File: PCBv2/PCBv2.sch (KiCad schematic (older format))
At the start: 76 parts, among them IC1 MAX743CWE+, J1 Arduino_Mega_Header, J10 Screw_Terminal_01x03, J11 Screw_Terminal_01x03, J12 Screw_Terminal_01x03, J13 Screw_Terminal_01x03, J2 Conn_01x10, J3 Conn_01x08, J4 Conn_01x08, J5 Conn_02x18_Odd_Even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

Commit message: Added photos of the prototype and changed the PCB
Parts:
- removed C20: 100nF, Cap:Cap, symbol C
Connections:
- net +15V: no longer U10.8 (V+)
- net -15V: no longer C19.2, U10.4 (V-)
- net 5V: now also C19.2, D5.1 (K), R20.2, R21.2, U10.8 (V+)
- net GND: now also U10.4 (V-)
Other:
- moved on the sheet: C19
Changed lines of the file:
@@
 L C C19
 U 1 1 5B011864
-P 10050 4750
-F 0 "C19" H 10075 4850 50  0000 L CNN
-F 1 "100nF" V 9900 4750 50  0000 L CNN
-F 2 "Cap:Cap" H 10088 4600 50  0001 C CNN
-F 3 "" H 10050 4750 50  0001 C CNN
-	1    10050 4750
-	0    1    1    0
+P 10050 5550
+F 0 "C19" H 10075 5650 50  0000 L CNN
+F 1 "100nF" V 9900 5550 50  0000 L CNN
+F 2 "Cap:Cap" H 10088 5400 50  0001 C CNN
+F 3 "" H 10050 5550 50  0001 C CNN
+	1    10050 5550
+	0    1    -1   0
 $EndComp
 Wire Wire Line
-	9900 4700 9900 4850
-Connection ~ 9900 4750
-Text Label 9900 4700 2    39   ~ 0
--15V
-Text Label 10200 4750 0    39   ~ 0
+	9900 5600 9900 5450
+Connection ~ 9900 5550
+Text Label 10200 5550 0    39   ~ 0
 GND
-$Comp
-L C C20
-U 1 1 5B011F3F
-P 10050 5500
-F 0 "C20" H 10075 5600 50  0000 L CNN
-F 1 "100nF" V 10200 5450 50  0000 L CNN
-F 2 "Cap:Cap" H 10088 5350 50  0001 C CNN
-F 3 "" H 10050 5500 50  0001 C CNN
-	1    10050 5500
-	0    1    1    0
-$EndComp
 Wire Wire Line
-	9900 5450 9900 5550
-Connection ~ 9900 5500
-Text Label 9900 5550 2    39   ~ 0
-+15V
-Text Label 10200 5500 0    39   ~ 0
-GND
+	9900 4850 9900 4750
 $Comp
 L R R23
@@
 	1    0    0    -1
 $EndComp
+Text Label 9900 4750 0    39   ~ 0
+GND
+Text Label 9900 5600 2    39   ~ 0
+5V
+Text Label 9150 5500 0    39   ~ 0
+5V
 $EndSCHEMATC

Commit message: Changes on PCB and pins of LCD
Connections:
- net PIN3: now also U1.2 (CE); no longer U1.1 (RST)
- net PIN4: now also U1.3 (DC); no longer U1.2 (CE)
- net PIN5: now also U1.4 (DIN); no longer U1.3 (DC)
- net PIN6: now also U1.5 (CLK); no longer U1.4 (DIN)
- net PIN2: now reaches J1.71 (PWM2/2)
- net PIN2: now also J3.6 (Pin_6), U1.1 (RST)
- removed net PIN7: J1.76 (PWM7/7), J3.1 (Pin_1), U1.5 (CLK)
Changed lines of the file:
@@
 Text Label 2500 950  0    39   ~ 0
 SDA
-Text Label 2500 1450 0    39   ~ 0
-PIN7
 Text Label 2500 1500 0    39   ~ 0
 PIN6
@@
 NoConn ~ 2200 1800
 NoConn ~ 2250 1750
-NoConn ~ 2200 1700
 NoConn ~ 2200 1350
 NoConn ~ 2250 1300
@@
 NoConn ~ 3050 2350
 NoConn ~ 3050 2250
-NoConn ~ 3050 2150
 Text Label 3050 2050 2    39   ~ 0
 PIN3
@@
 Text Label 3050 1750 2    39   ~ 0
 PIN6
-Text Label 3050 1650 2    39   ~ 0
-PIN7
 Text Label 3450 600  2    39   ~ 0
 SCL
@@
 $EndComp
 Text Label 6250 1100 2    39   ~ 0
+PIN2
+Text Label 6250 1200 2    39   ~ 0
 PIN3
-Text Label 6250 1200 2    39   ~ 0
+Text Label 6250 1300 2    39   ~ 0
 PIN4
-Text Label 6250 1300 2    39   ~ 0
+Text Label 6250 1400 2    39   ~ 0
 PIN5
-Text Label 6250 1400 2    39   ~ 0
+Text Label 6250 1500 2    39   ~ 0
 PIN6
-Text Label 6250 1500 2    39   ~ 0
-PIN7
 Text Label 6250 1600 2    39   ~ 0
 3.3V
@@
 Wire Wire Line
 	2200 950  2500 950
-Wire Wire Line
-	2250 1450 2500 1450
 Wire Wire Line
 	2200 1500 2500 1500
@@
 Text Label 9150 5500 0    39   ~ 0
 5V
+Wire Wire Line
+	2200 1700 2500 1700
+Text Label 2500 1700 0    39   ~ 0
+PIN2
+NoConn ~ 2250 1450
+NoConn ~ 3050 1650
+Text Label 3050 2150 2    39   ~ 0
+PIN2
 $EndSCHEMATC

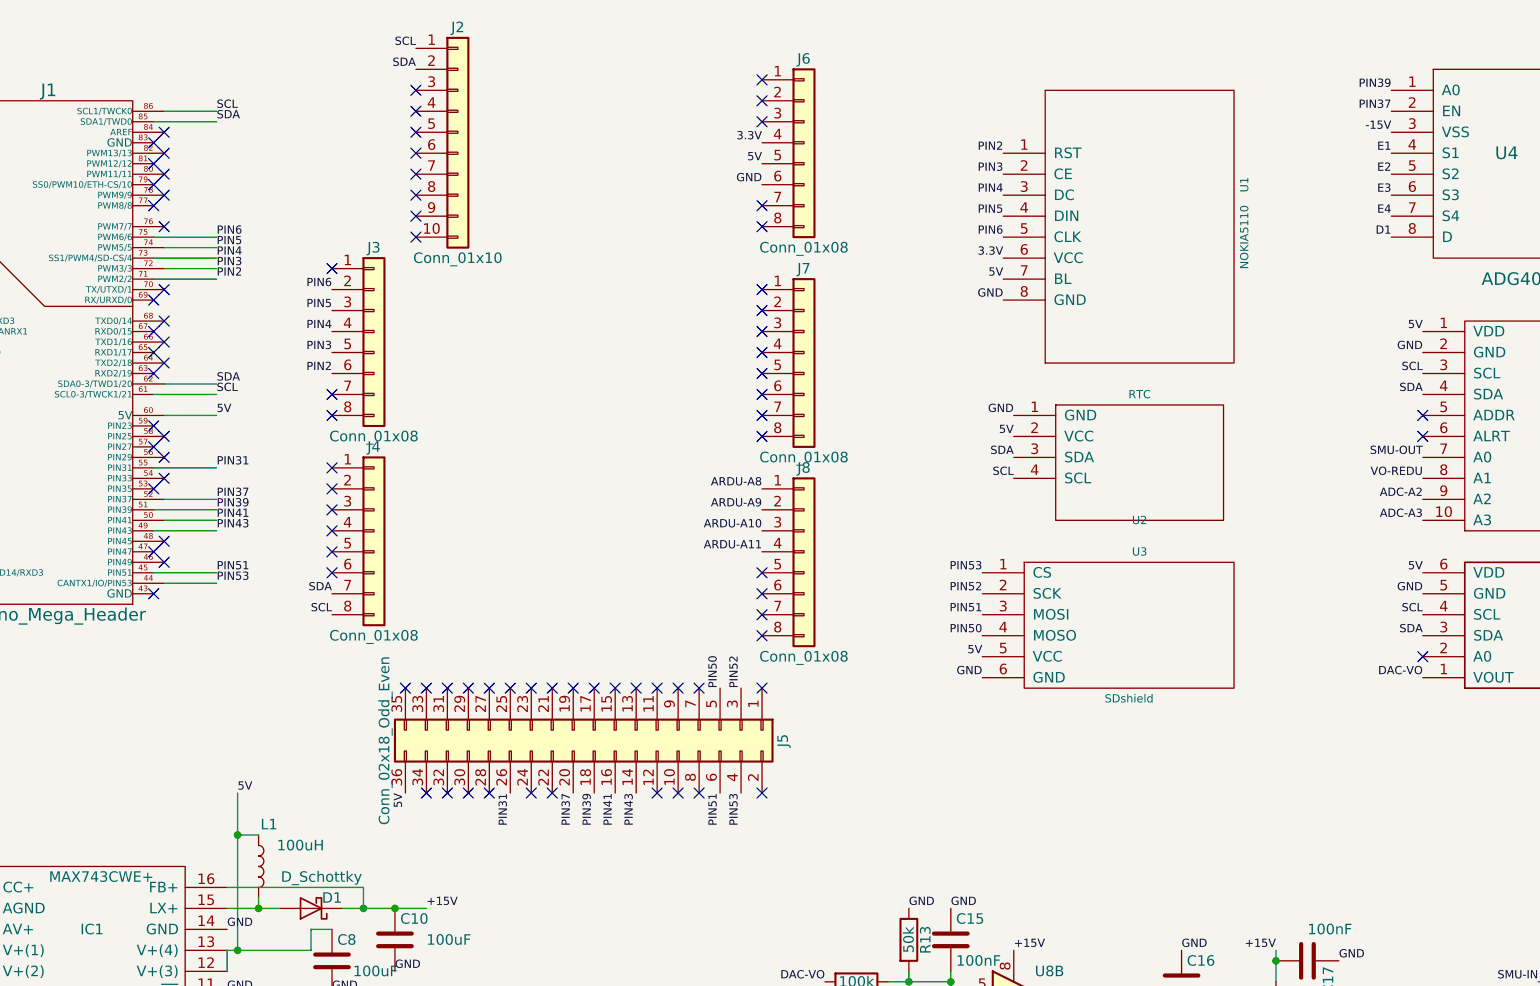
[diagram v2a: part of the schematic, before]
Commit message: Added GPRS communications and lots of changes on the main code!
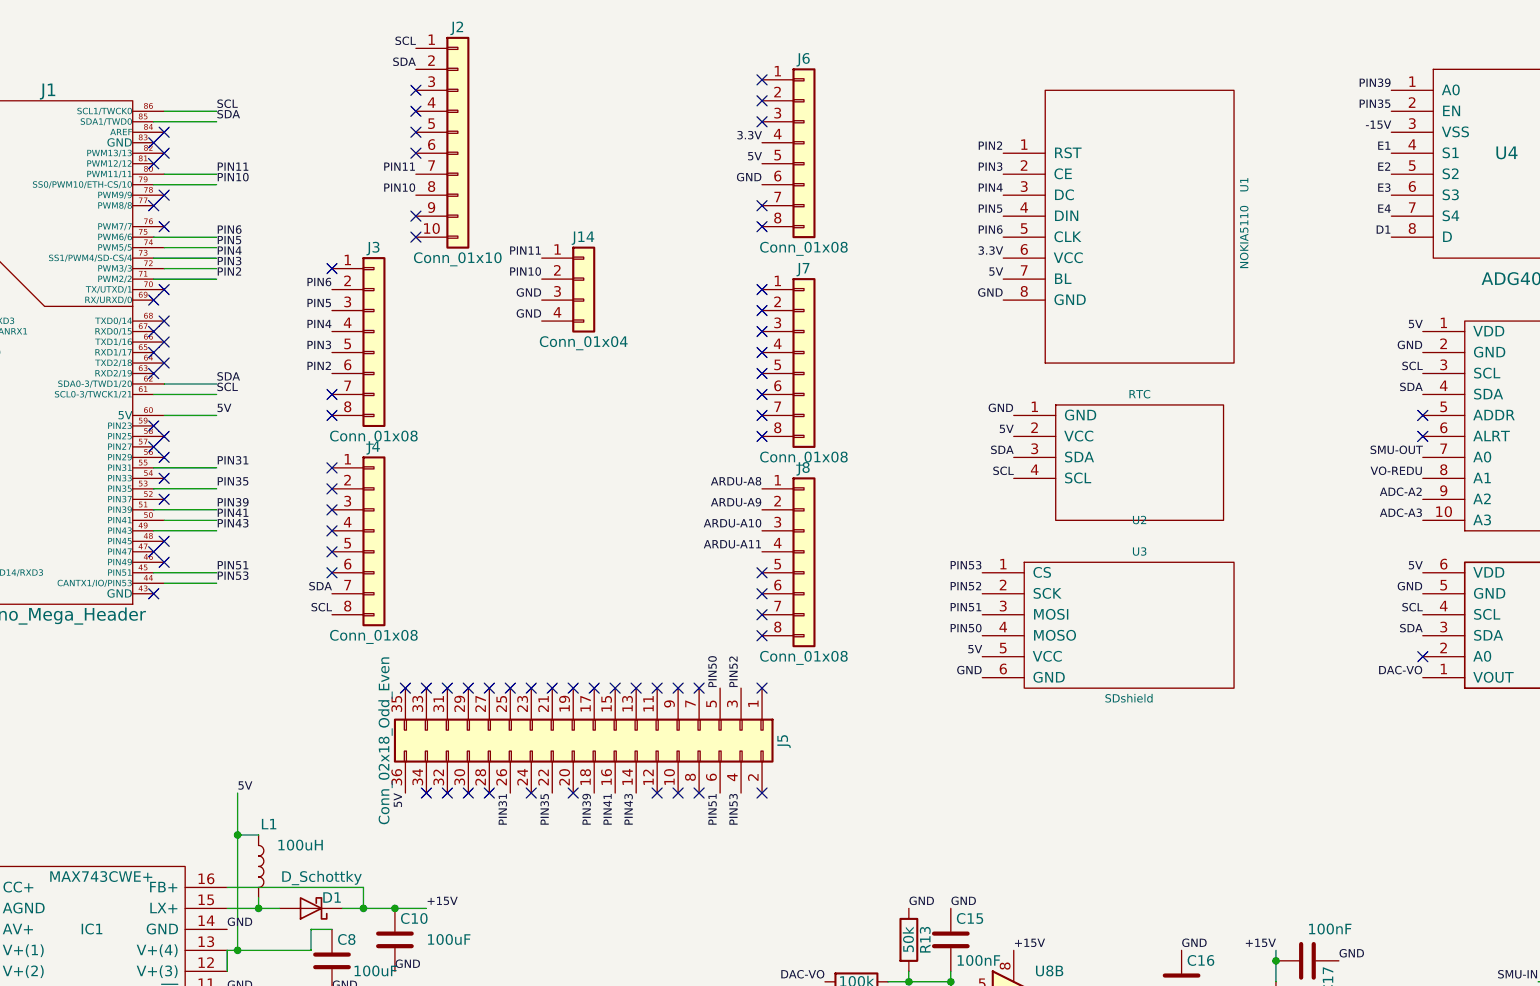
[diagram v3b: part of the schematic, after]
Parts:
- added J14: Conn_01x04, Pin_Headers:Pin_Header_Straight_1x04_Pitch2.54mm, symbol Conn_01x04
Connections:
- net GND: now also J14.3 (Pin_3), J14.4 (Pin_4)
- net PIN35: now reaches J1.53 (PIN35)
- net PIN35: now also J5.22 (Pin_22), U4.2 (EN)
- net PIN10: now reaches J1.79 (SS0/PWM10/ETH-CS/10)
- net PIN10: now also J2.8 (Pin_8), J14.2 (Pin_2)
- net PIN11: now reaches J1.80 (PWM11/11)
- net PIN11: now also J2.7 (Pin_7), J14.1 (Pin_1)
- removed net PIN37: J1.52 (PIN37), J5.20 (Pin_20), U4.2 (EN)
- no-connect marks 122 -> 118
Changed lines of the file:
@@
 Text Label 2500 2350 0    39   ~ 0
 5V
-Text Label 2500 2750 0    39   ~ 0
-PIN37
 Text Label 2500 2800 0    39   ~ 0
 PIN39
@@
 NoConn ~ 2200 3000
 NoConn ~ 2250 2950
-NoConn ~ 2200 2700
 NoConn ~ 2250 2650
 NoConn ~ 2250 2550
@@
 NoConn ~ 2200 1350
 NoConn ~ 2250 1300
-NoConn ~ 2200 1250
-NoConn ~ 2250 1200
 NoConn ~ 2200 1150
 NoConn ~ 2250 1100
@@
 Text Label 4400 4150 3    39   ~ 0
 PIN41
-Text Label 4200 4150 3    39   ~ 0
-PIN37
 Text Label 3900 4150 3    39   ~ 0
 PIN31
@@
 NoConn ~ 3800 4150
 NoConn ~ 4000 4150
-NoConn ~ 4100 4150
 $Comp
 L Conn_01x08 J4
@@
 NoConn ~ 3450 1000
 NoConn ~ 3450 1100
-NoConn ~ 3450 1200
-NoConn ~ 3450 1300
 $Comp
 L Conn_01x10 J2
@@
 Text Label 8100 800  2    39   ~ 0
 PIN39
-Text Label 8100 900  2    39   ~ 0
-PIN37
 Text Label 8100 1000 2    39   ~ 0
 -15V
@@
 Wire Wire Line
 	2200 2800 2500 2800
-Wire Wire Line
-	2250 2750 2500 2750
 Wire Wire Line
 	2250 2350 2500 2350
@@
 Text Label 3050 2150 2    39   ~ 0
 PIN2
+Wire Wire Line
+	2250 1200 2500 1200
+Wire Wire Line
+	2200 1250 2500 1250
+Text Label 2500 1200 0    39   ~ 0
+PIN11
+Text Label 2500 1250 0    39   ~ 0
+PIN10
+Text Label 4050 1600 2    39   ~ 0
+PIN11
+Text Label 4050 1700 2    39   ~ 0
+PIN10
+Text Label 4050 1800 2    39   ~ 0
+GND
+$Comp
+L Conn_01x04 J14
+U 1 1 5B0C0681
+P 4250 1700
+F 0 "J14" H 4250 1900 50  0000 C CNN
+F 1 "Conn_01x04" H 4250 1400 50  0000 C CNN
+F 2 "Pin_Headers:Pin_Header_Straight_1x04_Pitch2.54mm" H 4250 1700 50  0001 C CNN
+F 3 "" H 4250 1700 50  0001 C CNN
+	1    4250 1700
+	1    0    0    -1
+$EndComp
+Text Label 4050 1900 2    39   ~ 0
+GND
+Text Label 3450 1200 2    39   ~ 0
+PIN11
+Text Label 3450 1300 2    39   ~ 0
+PIN10
+NoConn ~ 2250 2750
+Wire Wire Line
+	2200 2700 2500 2700
+Text Label 2500 2700 0    39   ~ 0
+PIN35
+NoConn ~ 4200 4150
+Text Label 4100 4150 3    39   ~ 0
+PIN35
+Text Label 8100 900  2    39   ~ 0
+PIN35
 $EndSCHEMATC

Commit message: Added pwr pin of the SIM900 and documentation made
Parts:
- removed J14: Conn_01x04, Pin_Headers:Pin_Header_Straight_1x04_Pitch2.54mm, symbol Conn_01x04
- added J14: Conn_01x05, Pin_Headers:Pin_Header_Straight_1x05_Pitch2.54mm, symbol Conn_01x05
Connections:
- net GND: now also J14.4 (Pin_4), J14.5 (Pin_5)
- net PIN10: now also J14.2 (Pin_2)
- net PIN11: now also J14.1 (Pin_1)
- net PIN9: now reaches J1.78 (PWM9/9)
- net PIN9: now also J2.9 (Pin_9), J14.3 (Pin_3)
- no-connect marks 118 -> 116
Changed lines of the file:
@@
 NoConn ~ 2250 1750
 NoConn ~ 2200 1350
-NoConn ~ 2250 1300
 NoConn ~ 2200 1150
 NoConn ~ 2250 1100
@@
 	1    0    0    -1
 $EndComp
-NoConn ~ 3450 1400
 NoConn ~ 3450 1500
 NoConn ~ 5100 950
@@
 Text Label 4050 1700 2    39   ~ 0
 PIN10
-Text Label 4050 1800 2    39   ~ 0
-GND
-$Comp
-L Conn_01x04 J14
-U 1 1 5B0C0681
-P 4250 1700
-F 0 "J14" H 4250 1900 50  0000 C CNN
-F 1 "Conn_01x04" H 4250 1400 50  0000 C CNN
-F 2 "Pin_Headers:Pin_Header_Straight_1x04_Pitch2.54mm" H 4250 1700 50  0001 C CNN
-F 3 "" H 4250 1700 50  0001 C CNN
-	1    4250 1700
-	1    0    0    -1
-$EndComp
 Text Label 4050 1900 2    39   ~ 0
+GND
+Text Label 4050 2000 2    39   ~ 0
 GND
 Text Label 3450 1200 2    39   ~ 0
@@
 Text Label 8100 900  2    39   ~ 0
 PIN35
+Wire Wire Line
+	2250 1300 2500 1300
+Text Label 2500 1300 0    39   ~ 0
+PIN9
+Text Label 3450 1400 2    39   ~ 0
+PIN9
+$Comp
+L Conn_01x05 J14
+U 1 1 5B15155E
+P 4250 1800
+F 0 "J14" H 4250 2100 50  0000 C CNN
+F 1 "Conn_01x05" H 4250 1500 50  0000 C CNN
+F 2 "Pin_Headers:Pin_Header_Straight_1x05_Pitch2.54mm" H 4250 1800 50  0001 C CNN
+F 3 "" H 4250 1800 50  0001 C CNN
+	1    4250 1800
+	1    0    0    -1
+$EndComp
+Text Label 4050 1800 2    39   ~ 0
+PIN9
 $EndSCHEMATC

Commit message: Added output via terminal and voltage sweep for I/V curves with the SMU
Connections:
- net -15V: now also IC1.9 (FB-)
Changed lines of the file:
@@
 Text Label 4050 1800 2    39   ~ 0
 PIN9
+Wire Wire Line
+	2550 5300 3150 5300
+Wire Wire Line
+	3150 5300 3150 5200
+Connection ~ 3150 5200
 $EndSCHEMATC

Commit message: Added some missing images for the latex thesis and small changes in code
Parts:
- R10, R11: value 10k -> 100k
- R20: value 22k -> 10k
- R21: value 1k -> 100k
- R22: value 330 -> 33k
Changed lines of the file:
@@
 P 4750 5650
 F 0 "R10" V 4830 5650 50  0000 C CNN
-F 1 "10k" V 4750 5650 50  0000 C CNN
+F 1 "100k" V 4750 5650 50  0000 C CNN
 F 2 "TH-R:R-C-L-D" V 4680 5650 50  0001 C CNN
 F 3 "" H 4750 5650 50  0001 C CNN
@@
 P 5250 5200
 F 0 "R11" V 5330 5200 50  0000 C CNN
-F 1 "10k" V 5250 5200 50  0000 C CNN
+F 1 "100k" V 5250 5200 50  0000 C CNN
 F 2 "TH-R:R-C-L-D" V 5180 5200 50  0001 C CNN
 F 3 "" H 5250 5200 50  0001 C CNN
@@
 P 9000 5500
 F 0 "R20" V 9080 5500 50  0000 C CNN
-F 1 "22k" V 9000 5500 50  0000 C CNN
+F 1 "10k" V 9000 5500 50  0000 C CNN
 F 2 "TH-R:R-C-L-D" V 8930 5500 50  0001 C CNN
 F 3 "" H 9000 5500 50  0001 C CNN
@@
 P 9400 5500
 F 0 "R21" V 9480 5500 50  0000 C CNN
-F 1 "1k" V 9400 5500 50  0000 C CNN
+F 1 "100k" V 9400 5500 50  0000 C CNN
 F 2 "TH-R:R-C-L-D" V 9330 5500 50  0001 C CNN
 F 3 "" H 9400 5500 50  0001 C CNN
@@
 P 9600 5700
 F 0 "R22" V 9680 5700 50  0000 C CNN
-F 1 "330" V 9600 5700 50  0000 C CNN
+F 1 "33k" V 9600 5700 50  0000 C CNN
 F 2 "TH-R:R-C-L-D" V 9530 5700 50  0001 C CNN
 F 3 "" H 9600 5700 50  0001 C CNN
